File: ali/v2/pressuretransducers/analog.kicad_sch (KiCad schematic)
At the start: 82 parts, among them J10 Conn_01x02, J11 Conn_01x02, J12 Conn_01x02, J13 Conn_01x02, J14 Conn_01x02, J15 Conn_01x02, J8 Conn_01x02, J9 Conn_01x02, U5 ADS131M08IRSN, Y3 8.192 MHz

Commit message: Minor updates
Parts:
- removed C35, C36: 15pF, APRL_Passive:C_0603, symbol Device:C_Small
- removed Y3: 8.192 MHz, APRL_Passive:3225-4P-L, symbol Device:Crystal_GND24
- renumbered C37 to C30, C40 to C31, C39 to C32, C42 to C33, C38 to C34, C41 to C35, C29 to C36, C30 to C37, C31 to C38, C34 to C39, C32 to C40, C43 to C41, C46 to C42, C45 to C43, C48 to C44, C44 to C45, C47 to C46, C49 to C47, C52 to C48, C51 to C49, C54 to C50, C50 to C51, C53 to C52, C33 to C53, C55 to C54, C58 to C55, C57 to C56, C60 to C57, C56 to C58, J8 to J10, J9 to J11, J10 to J12, J11 to J13, J12 to J14, J13 to J15, J14 to J16, J15 to J17, R20 to R19, R23 to R20, R19 to R21, R21 to R23, R26 to R25, R29 to R26, R25 to R27, R27 to R29, R32 to R31, R35 to R32, R31 to R33, R33 to R35, R38 to R37, R41 to R38, R37 to R39, R39 to R41
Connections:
- net CLK: now reaches U5.23 (XTAL1/CLKIN)
- no-connect marks 0 -> 1
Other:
- note removed: "8 MHz is more available and there's not really any losses so I'm not sure if this should be swapped"

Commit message: Globally remove LCSC labels, update MPNs and IOCs, add +5V monitoring to DAQs, fix some footprints
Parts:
- C30, C31, C34, C35, C41, C42, C45, C46, C47, C48, C51, C52, C54, C55, C58, C59: MPN GRM21B5C2J102FWA3 -> GRM1885C1H102FA01
- C32, C33, C43, C44, C49, C50, C56, C57: MPN GRM21B5C2E103FWAA -> GRM1885C1H103JA01
- C53: MPN GRM21AR72A224KAC5 -> GRM188R71H224KAC4
- D10, D11, D12, D13, D6, D7, D8, D9: MPN SMF7V0A -> SMF7V0A-E3-18
- renumbered R19 to R21, R20 to R22, R21 to R23, R22 to R24, R23 to R25, R24 to R26, R25 to R27, R26 to R28, R27 to R29, R28 to R30, R29 to R31, R30 to R32, R31 to R33, R32 to R34, R33 to R35, R34 to R36, R35 to R37, R36 to R38, R37 to R39, R38 to R40, R39 to R41, R40 to R42, R41 to R43, R42 to R44
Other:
- note added: "INPUTS"
- moved on the sheet: C30, C31, C32, C33, C34, C35, C36, C37, C38, C39, C40, C41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

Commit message: Small documentation
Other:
- note added: "ADC"
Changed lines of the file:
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@@
+		)
+	)
+	(text "ADC"
+		(exclude_from_sim no)
+		(at 190.246 48.26 0)
+		(effects
+			(font
+				(size 3.81 3.81)
+			)
 		)
 	)

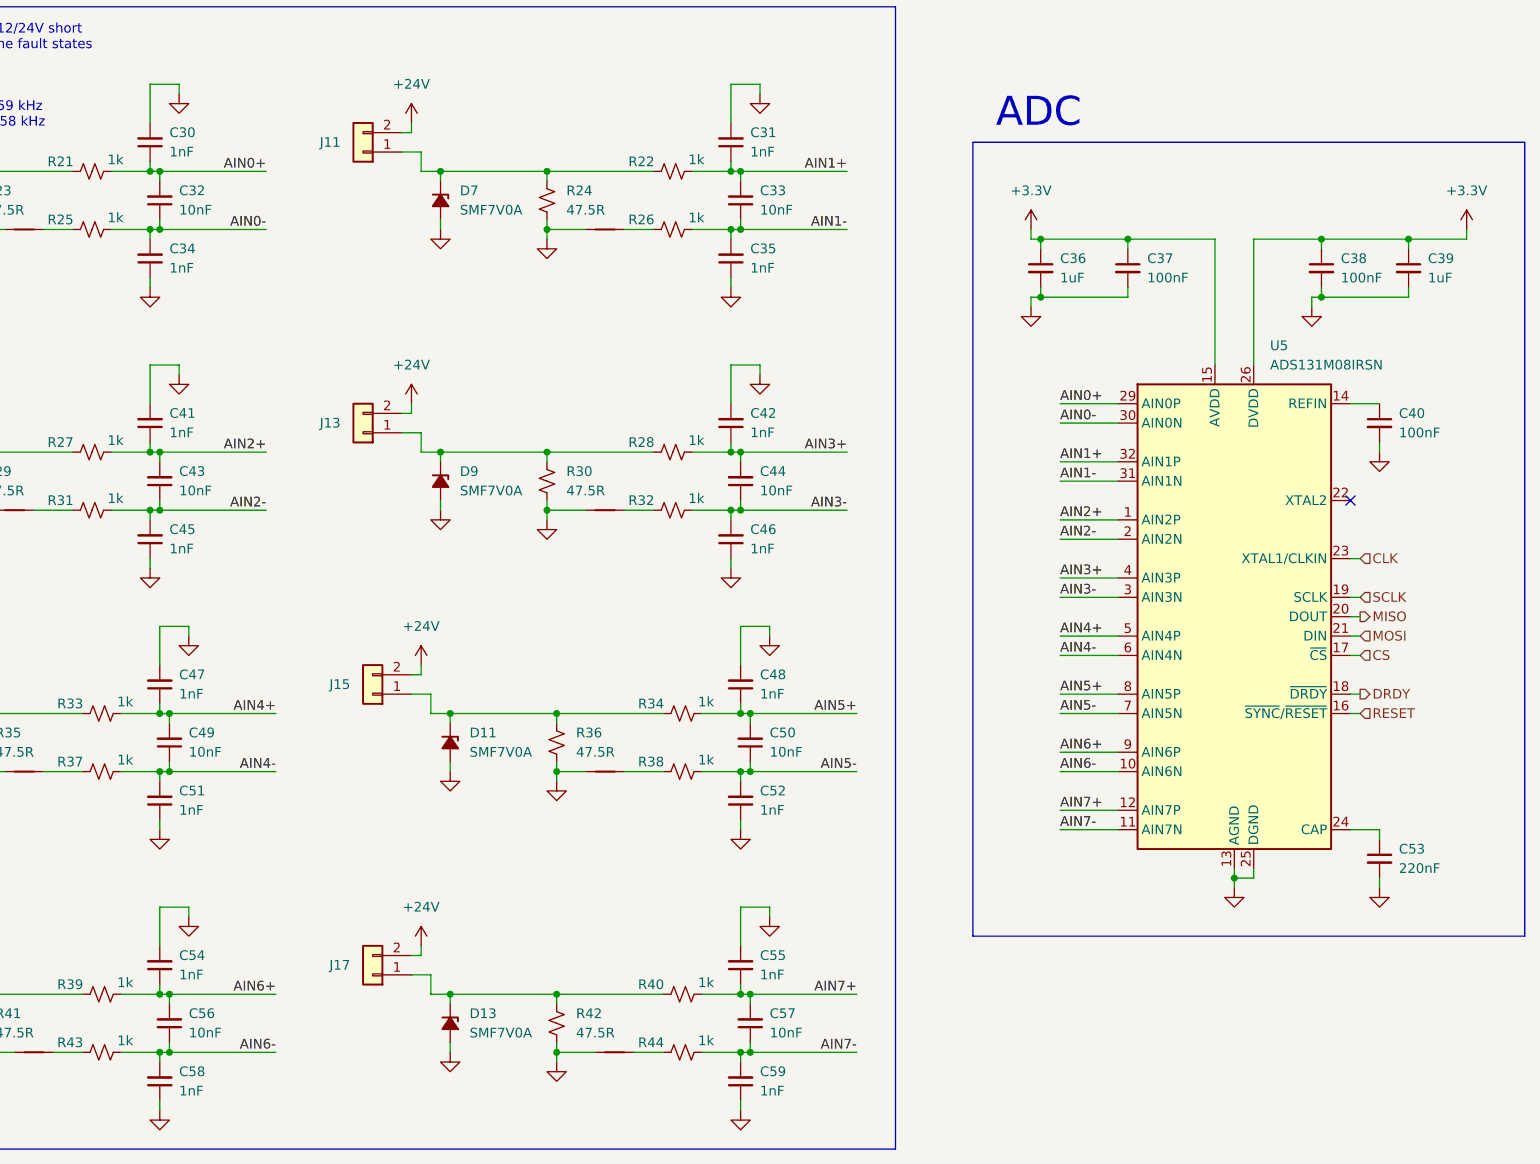
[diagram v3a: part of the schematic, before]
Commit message: the great flatpak and kicad 10.0.6 migration
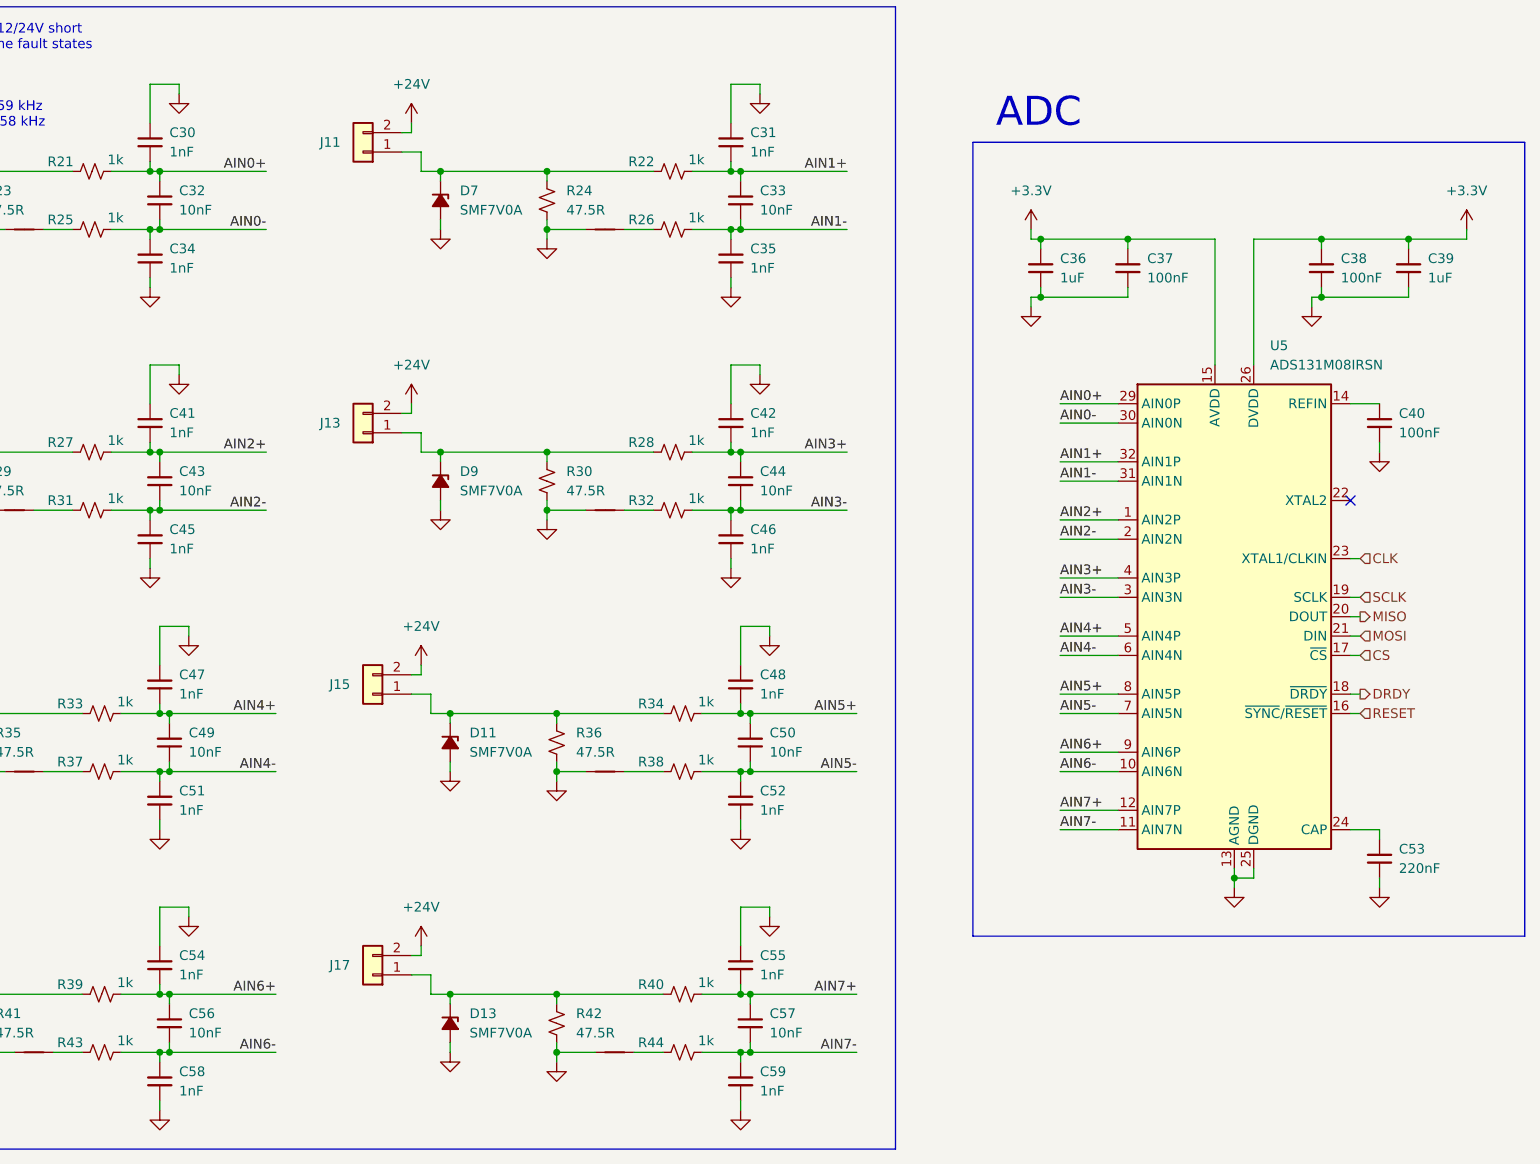
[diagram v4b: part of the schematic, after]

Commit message: The other half of the great 10.0.6 migration
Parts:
- U5: symbol Analog_ADC:ADS131M08xPBS -> APRL_Analog:ADS131M08IRSN
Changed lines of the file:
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@@
 	)
 	(symbol
-		(lib_id "Analog_ADC:ADS131M08xPBS")
+		(lib_id "APRL_Analog:ADS131M08IRSN")
 		(at 215.9 114.3 0)
 		(unit 1)
@@
 			)
 		)
-		(property "Description" "8-Channel, Simultaneously-Sampling, 24-Bit, Delta-Sigma ADC"
+		(property "Description" "8-channel, 24-bit, simultaneous-sampling delta-sigma ADC, 32 kSPS, PGA 1-128, SPI, WQFN-32 with thermal pad (Texas RSN)"
 			(at 276.86 175.26 0)
 			(hide yes)

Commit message: Add more commentary
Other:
- note added: "It would be trivial to isolate this entire board using the same trick we used on the thermocouple board, where we just place a dc/dc isolator chip on the +5V rail. This would enhance the protection of our system by allowing us to isolate +24V, which would prevent ground bounce and greatly limit damage from shorts because there is no return line back to the power supply if its ground is floating. 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"
- note added: "Still need to double check that 47.5R is good"
- note added: "The idea behind the net ties is to create a kelvin connection but I don't think I'm really achieving it here and I don't think that it'd actually help if I did"
- note added: "The protection diode and shunt resistor are going to immediately blow and/or short if this thing actually got shorted, but I'm not sure if we want a PTC on every input, especially since it'd mean there'd be a nontrivial change in DC resistance relative to the shunt. That being said, it shouldn't affect us if we placed it on the high side, though."
- note added: "The voltage drop over these 1K resistors is nontrivial but can be calibrated out"
- note added: "These caps are all c0g and these resistors are all thin film. I started placing MPN and Manufacturer on the fields of nearly every part on these boards so that we can standardize on certain parts and to make ordering easier, and to prevent the TC situation where we used X5Rs for the DM filtering on the AFE"
- note added: "These connectors were colored by claude which is why they're off I did search for connectors that are not just gray but they simply do not exist"
- note added: "This diode is a jellybean part but I'm not sure if this is ideal"
- moved on the sheet: C40
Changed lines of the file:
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@@
 		)
 	)
+	(text "Still need to double check that 47.5R is good"
+		(exclude_from_sim no)
+		(at 119.888 179.832 0)
+		(effects
+			(font
+				(size 1.27 1.27)
+			)
+		)
+	)
+	(text "The protection diode and shunt resistor are going to immediately blow and/or short if\nthis thing actually got shorted, but I'm not sure if we want a PTC on every input,\nespecially since it'd mean there'd be a nontrivial change in DC resistance relative to the shunt. That being said,\nit shouldn't affect us if we placed it on the high side, though."
+		(exclude_from_sim no)
+		(at -40.894 89.408 0)
+		(effects
+			(font
+				(size 1.27 1.27)
+			)
+		)
+	)
+	(text "These connectors were colored by claude which is why they're off\nI did search for connectors that are not just gray but they simply\ndo not exist"
+		(exclude_from_sim no)
+		(at -17.526 56.134 0)
+		(effects
+			(font
+				(size 1.27 1.27)
+			)
+		)
+	)
 	(text "INPUTS"
 		(exclude_from_sim no)
@@
 		)
 	)
+	(text "It would be trivial to isolate this entire board using the same trick we used on the thermocouple board,\nwhere we just place a dc/dc isolator chip on the +5V rail. This would enhance the protection of our system\nby allowing us to isolate +24V, which would prevent ground bounce and greatly limit damage from shorts because\nthere is no return line back to the power supply if its ground is floating. This was omitted for now, as we agreed."
+		(exclude_from_sim no)
+		(at 112.522 28.448 0)
+		(effects
+			(font
+				(size 1.27 1.27)
+			)
+		)
+	)
+	(text "The voltage drop over these 1K resistors is nontrivial but can be calibrated out"
+		(exclude_from_sim no)
+		(at 44.704 73.152 0)
+		(effects
+			(font
+				(size 1.27 1.27)
+			)
+		)
+	)
 	(text "ADC"
 		(exclude_from_sim no)
@@
 		)
 	)
+	(text "These caps are all c0g and these resistors are all thin film. I started placing MPN and Manufacturer\non the fields of nearly every part on these boards so that we can standardize on certain parts\nand to make ordering easier, and to prevent the TC situation where we used X5Rs for the DM filtering\non the AFE"
+		(exclude_from_sim no)
+		(at 136.144 77.47 0)
+		(effects
+			(font
+				(size 1.27 1.27)
+			)
+		)
+	)
 	(text "fcm = 159 kHz\nfdm = 7.58 kHz"
 		(exclude_from_sim no)
@@
 		)
 	)
+	(text "The idea behind the net ties is to create a kelvin connection but I don't think I'm really\nachieving it here and I don't think that it'd actually help if I did"
+		(exclude_from_sim no)
+		(at 63.246 189.484 0)
+		(effects
+			(font
+				(size 1.27 1.27)
+			)
+		)
+	)
 	(text "Should be able to handle +12/24V short\nUse NAMUR NE43 to determine fault states"
 		(exclude_from_sim no)
@@
 		)
 	)
+	(text "This diode is a jellybean part but I'm not sure if this is ideal"
+		(exclude_from_sim no)
+		(at 113.03 141.732 0)
+		(effects
+			(font
+				(size 1.27 1.27)
+			)
+		)
+	)
 	(junction
 		(at 36.83 163.83)
@@
 	(wire
 		(pts
-			(xy 234.95 91.44) (xy 234.95 92.71)
+			(xy 234.95 92.71) (xy 234.95 93.98)
 		)
 		(stroke
@@
 	(wire
 		(pts
+			(xy 234.95 86.36) (xy 231.14 86.36)
+		)
+		(stroke
+			(width 0)
+			(type default)
+		)
+	)
+	(wire
+		(pts
 			(xy 76.2 134.62) (xy 90.17 134.62)
 		)
@@
 	(wire
 		(pts
-			(xy 231.14 86.36) (xy 234.95 86.36)
+			(xy 144.78 92.71) (xy 149.86 92.71)
 		)
 		(stroke
@@
 	(wire
 		(pts
-			(xy 144.78 92.71) (xy 149.86 92.71)
+			(xy 151.13 115.57) (xy 151.13 120.65)
 		)
 		(stroke
@@
 	(wire
 		(pts
-			(xy 151.13 115.57) (xy 151.13 120.65)
+			(xy 152.4 127) (xy 152.4 128.27)
 		)
 		(stroke
@@
 	(wire
 		(pts
-			(xy 152.4 127) (xy 152.4 128.27)
+			(xy 154.94 152.4) (xy 151.13 152.4)
 		)
 		(stroke
@@
 	(wire
 		(pts
-			(xy 154.94 152.4) (xy 151.13 152.4)
+			(xy 190.5 72.39) (xy 201.93 72.39)
 		)
 		(stroke
@@
 	(wire
 		(pts
-			(xy 190.5 72.39) (xy 201.93 72.39)
+			(xy 234.95 87.63) (xy 234.95 86.36)
 		)
 		(stroke
@@
 	(symbol
 		(lib_id "power:GND")
-		(at 234.95 92.71 0)
+		(at 234.95 93.98 0)
 		(unit 1)
 		(body_style 1)
@@
 		(fields_autoplaced yes)
 		(property "Reference" "#PWR080"
-			(at 234.95 99.06 0)
+			(at 234.95 100.33 0)
 			(hide yes)
 			(show_name no)
@@
 		)
 		(property "Value" "GND"
-			(at 234.95 97.79 0)
+			(at 234.95 99.06 0)
 			(hide yes)
 			(show_name no)
@@
 		)
 		(property "Footprint" ""
-			(at 234.95 92.71 0)
+			(at 234.95 93.98 0)
 			(hide yes)
 			(show_name no)
@@
 		)
 		(property "Datasheet" ""
-			(at 234.95 92.71 0)
+			(at 234.95 93.98 0)
 			(hide yes)
 			(show_name no)
@@
 		)
 		(property "Description" "Power symbol creates a global label with name \"GND\" , ground"
-			(at 234.95 92.71 0)
+			(at 234.95 93.98 0)
 			(hide yes)
 			(show_name no)
@@
 	(symbol
 		(lib_id "Device:C_Small")
-		(at 234.95 88.9 0)
+		(at 234.95 90.17 0)
 		(unit 1)
 		(body_style 1)
@@
 		(fields_autoplaced yes)
 		(property "Reference" "C40"
-			(at 237.49 87.6362 0)
+			(at 237.49 88.9062 0)
 			(show_name no)
 			(do_not_autoplace no)
@@
 		)
 		(property "Value" "100nF"
-			(at 237.49 90.1762 0)
+			(at 237.49 91.4462 0)
 			(show_name no)
 			(do_not_autoplace no)
@@
 		)
 		(property "Footprint" "APRL_Passive:C_0603"
-			(at 234.95 88.9 0)
+			(at 234.95 90.17 0)
 			(hide yes)
 			(show_name no)
@@
 		)
 		(property "Datasheet" ""
-			(at 234.95 88.9 0)
+			(at 234.95 90.17 0)
 			(hide yes)
 			(show_name no)
@@
 		)
 		(property "Description" "Unpolarized capacitor, small symbol"
-			(at 234.95 88.9 0)
+			(at 234.95 90.17 0)
 			(hide yes)
 			(show_name no)
@@
 		)
 		(property "MPN" "GRM188R72A104KA35"
-			(at 234.95 88.9 0)
+			(at 234.95 90.17 0)
 			(hide yes)
 			(show_name no)
@@
 		)
 		(property "MANUFACTURER" "Murata"
-			(at 234.95 88.9 0)
+			(at 234.95 90.17 0)
 			(hide yes)
 			(show_name no)

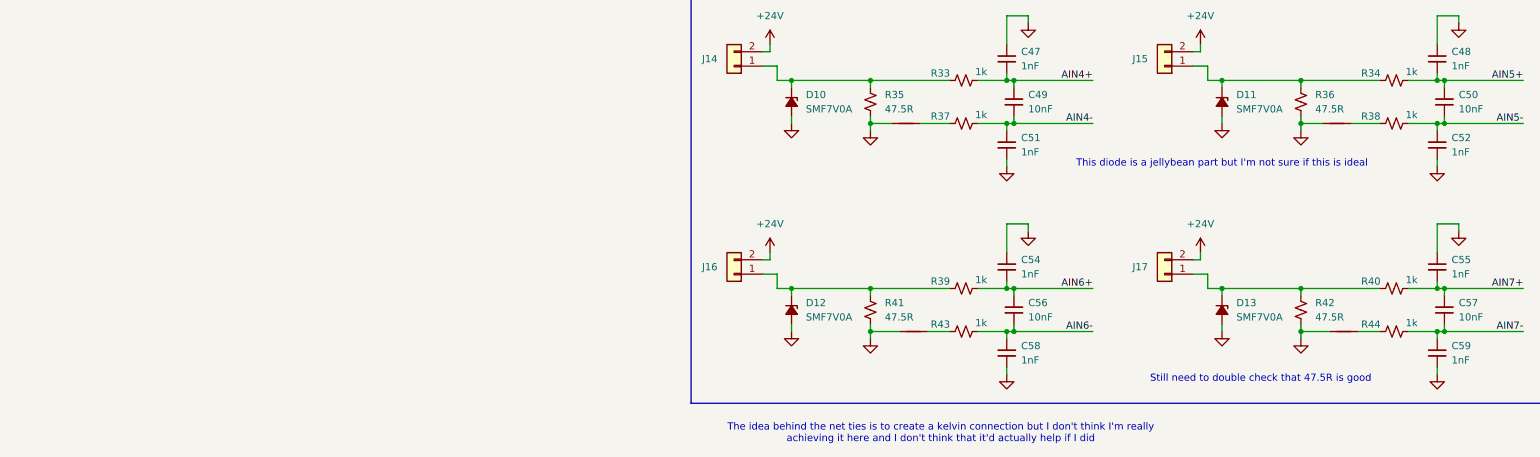
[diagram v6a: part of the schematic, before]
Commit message: Document setup, update template, and use an ampersand when referring to APRL
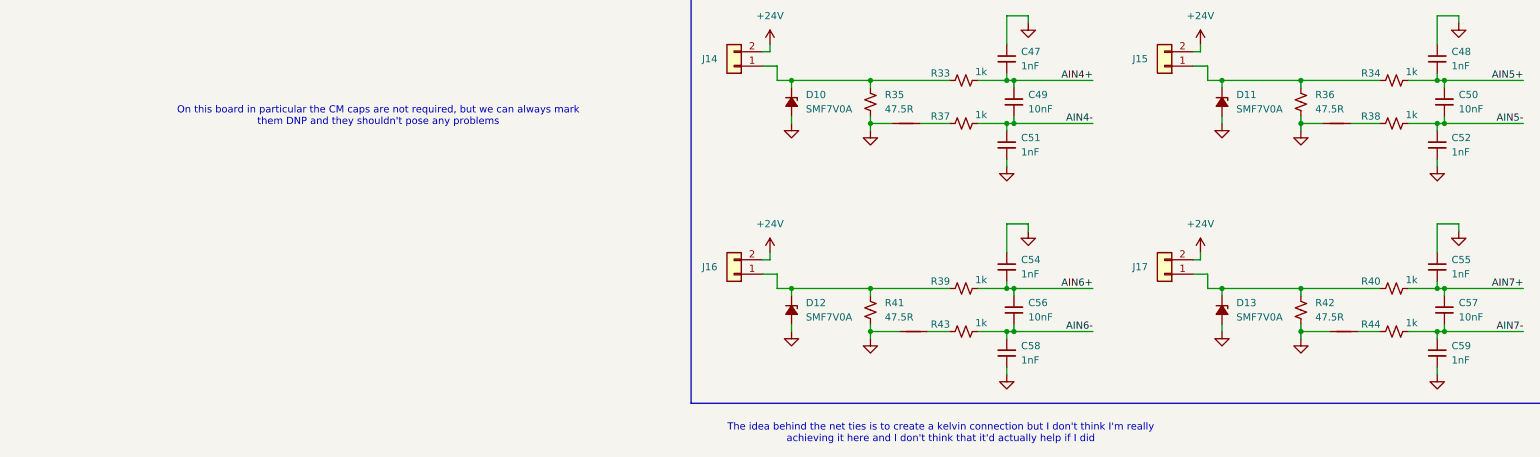
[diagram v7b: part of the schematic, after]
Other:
- note added: "On this board in particular the CM caps are not required, but we can always mark them DNP and they shouldn't pose any problems"
- note removed: "Still need to double check that 47.5R is good"
- note removed: "This diode is a jellybean part but I'm not sure if this is ideal"
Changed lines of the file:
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@@
-		)
-	)
-	(text "Still need to double check that 47.5R is good"
-		(exclude_from_sim no)
-		(at 119.888 179.832 0)
-		(effects
-			(font
-				(size 1.27 1.27)
-			)
 		)
 	)
@@
 		)
 	)
-	(text "This diode is a jellybean part but I'm not sure if this is ideal"
+	(text "On this board in particular the CM caps are not required, but we can always mark\nthem DNP and they shouldn't pose any problems"
 		(exclude_from_sim no)
-		(at 113.03 141.732 0)
+		(at -36.322 133.35 0)
 		(effects
 			(font
